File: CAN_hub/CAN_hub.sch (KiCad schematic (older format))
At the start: 8 parts, among them J1 Conn_01x04_Male, J2 Conn_01x04_Male, J3 Conn_01x04_Male, J4 Conn_01x04_Male, J5 Conn_01x04_Male, J6 Conn_01x04_Male, J7 Conn_01x04_Male, J8 Conn_01x04_Male

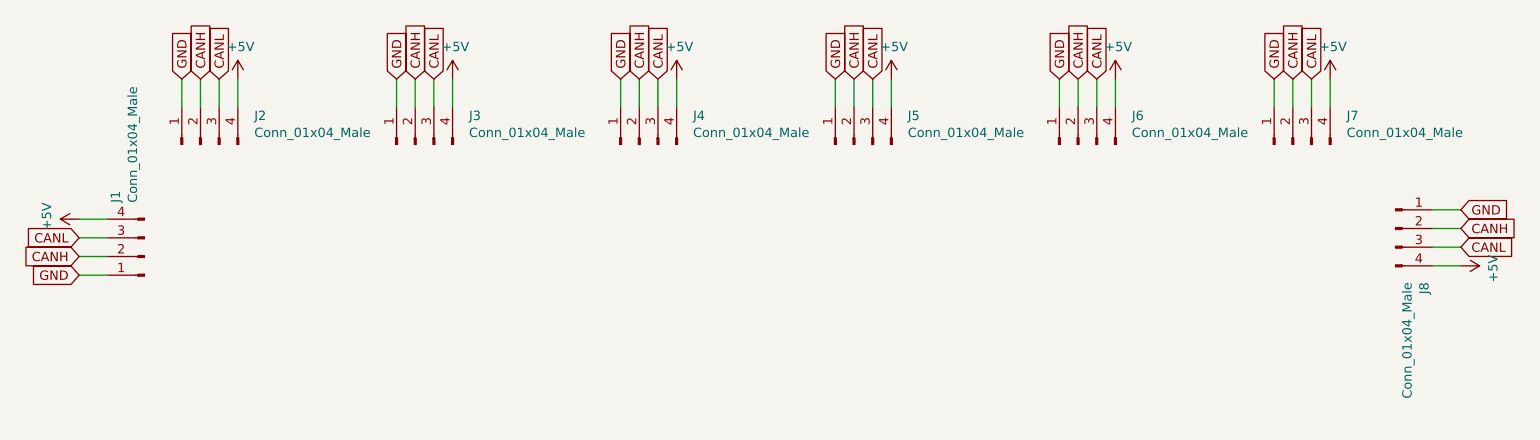
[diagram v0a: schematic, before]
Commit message: Updated shematic and layout to accomodate changes from first round of testing
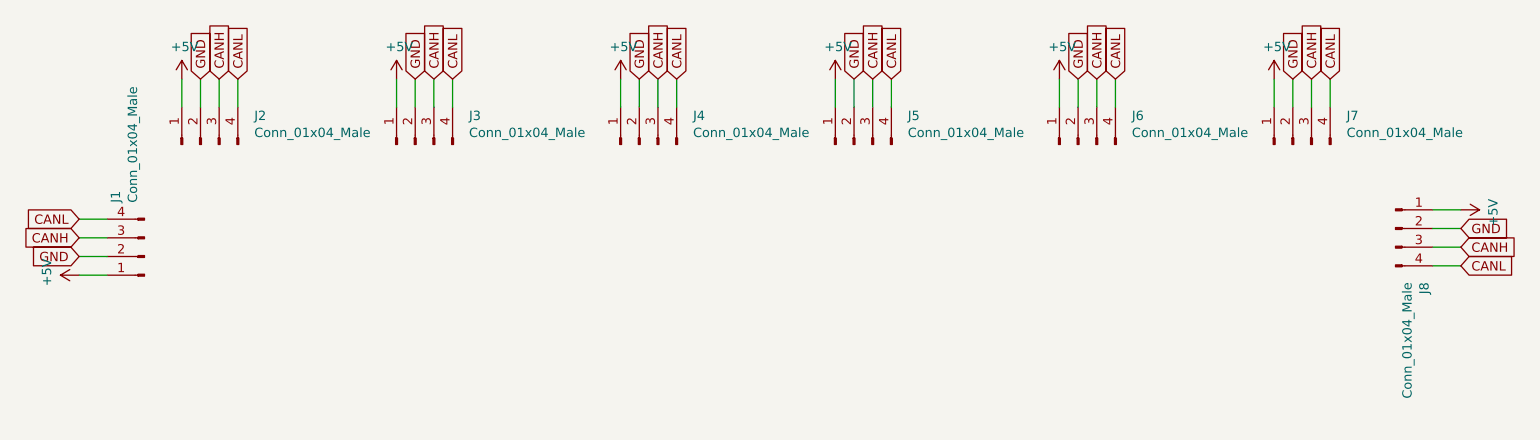
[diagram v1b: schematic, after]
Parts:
- J1, J2, J3, J4, J5, J6, J7, J8: footprint Connector_PinHeader_1.00mm:PinHeader_1x04_P1.00mm_Vertical -> Connector_JST:JST_EH_B4B-EH-A_1x04_P2.50mm_Vertical
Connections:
- net +5V: now also J1.1 (Pin_1), J2.1 (Pin_1), J3.1 (Pin_1), J4.1 (Pin_1), J5.1 (Pin_1), J6.1 (Pin_1), J7.1 (Pin_1), J8.1 (Pin_1); no longer J1.4 (Pin_4), J2.4 (Pin_4), J3.4 (Pin_4), J4.4 (Pin_4), J5.4 (Pin_4), J6.4 (Pin_4), J7.4 (Pin_4), J8.4 (Pin_4)
- net CANH: now also J1.3 (Pin_3), J2.3 (Pin_3), J3.3 (Pin_3), J4.3 (Pin_3), J5.3 (Pin_3), J6.3 (Pin_3), J7.3 (Pin_3), J8.3 (Pin_3); no longer J1.2 (Pin_2), J2.2 (Pin_2), J3.2 (Pin_2), J4.2 (Pin_2), J5.2 (Pin_2), J6.2 (Pin_2), J7.2 (Pin_2), J8.2 (Pin_2)
- net CANL: now also J1.4 (Pin_4), J2.4 (Pin_4), J3.4 (Pin_4), J4.4 (Pin_4), J5.4 (Pin_4), J6.4 (Pin_4), J7.4 (Pin_4), J8.4 (Pin_4); no longer J1.3 (Pin_3), J2.3 (Pin_3), J3.3 (Pin_3), J4.3 (Pin_3), J5.3 (Pin_3), J6.3 (Pin_3), J7.3 (Pin_3), J8.3 (Pin_3)
- net GND: now also J1.2 (Pin_2), J2.2 (Pin_2), J3.2 (Pin_2), J4.2 (Pin_2), J5.2 (Pin_2), J6.2 (Pin_2), J7.2 (Pin_2), J8.2 (Pin_2); no longer J1.1 (Pin_1), J2.1 (Pin_1), J3.1 (Pin_1), J4.1 (Pin_1), J5.1 (Pin_1), J6.1 (Pin_1), J7.1 (Pin_1), J8.1 (Pin_1)
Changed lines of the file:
@@
 EESchema Schematic File Version 4
-LIBS:CAN_8_connectors-cache
+LIBS:CAN_hub-cache
 EELAYER 30 0
 EELAYER END
@@
 Wire Wire Line
 	3700 2600 3700 2750
-Text GLabel 3700 2600 1    50   Input ~ 0
+Text GLabel 3800 2600 1    50   Input ~ 0
 GND
 $Comp
@@
 F 0 "J3" V 3954 2662 50  0000 R CNN
 F 1 "Conn_01x04_Male" V 3863 2662 50  0000 R CNN
-F 2 "Connector_PinHeader_1.00mm:PinHeader_1x04_P1.00mm_Vertical" H 3800 2950 50  0001 C CNN
+F 2 "Connector_JST:JST_EH_B4B-EH-A_1x04_P2.50mm_Vertical" H 3800 2950 50  0001 C CNN
 F 3 "~" H 3800 2950 50  0001 C CNN
 	1    3800 2950
 	0    -1   -1   0
 $EndComp
-Text GLabel 3800 2600 1    50   Input ~ 0
-CANH
 Text GLabel 3900 2600 1    50   Input ~ 0
+CANH
+Text GLabel 4000 2600 1    50   Input ~ 0
 CANL
 Wire Wire Line
@@
 L power:+5V #PWR03
 U 1 1 5E38804E
-P 4000 2600
-F 0 "#PWR03" H 4000 2450 50  0001 C CNN
-F 1 "+5V" H 4015 2773 50  0000 C CNN
-F 2 "" H 4000 2600 50  0001 C CNN
-F 3 "" H 4000 2600 50  0001 C CNN
-	1    4000 2600
+P 3700 2600
+F 0 "#PWR03" H 3700 2450 50  0001 C CNN
+F 1 "+5V" H 3715 2773 50  0000 C CNN
+F 2 "" H 3700 2600 50  0001 C CNN
+F 3 "" H 3700 2600 50  0001 C CNN
+	1    3700 2600
 	1    0    0    -1
 $EndComp
 Wire Wire Line
 	4000 2600 4000 2750
-Text GLabel 2550 2600 1    50   Input ~ 0
-GND
 Text GLabel 2650 2600 1    50   Input ~ 0
-CANH
+GND
 Text GLabel 2750 2600 1    50   Input ~ 0
+CANH
+Text GLabel 2850 2600 1    50   Input ~ 0
 CANL
 $Comp
 L power:+5V #PWR02
 U 1 1 5E370C49
-P 2850 2600
-F 0 "#PWR02" H 2850 2450 50  0001 C CNN
-F 1 "+5V" H 2865 2773 50  0000 C CNN
-F 2 "" H 2850 2600 50  0001 C CNN
-F 3 "" H 2850 2600 50  0001 C CNN
-	1    2850 2600
+P 2550 2600
+F 0 "#PWR02" H 2550 2450 50  0001 C CNN
+F 1 "+5V" H 2565 2773 50  0000 C CNN
+F 2 "" H 2550 2600 50  0001 C CNN
+F 3 "" H 2550 2600 50  0001 C CNN
+	1    2550 2600
 	1    0    0    -1
 $EndComp
@@
 F 0 "J2" V 2804 2662 50  0000 R CNN
 F 1 "Conn_01x04_Male" V 2713 2662 50  0000 R CNN
-F 2 "Connector_PinHeader_1.00mm:PinHeader_1x04_P1.00mm_Vertical" H 2650 2950 50  0001 C CNN
+F 2 "Connector_JST:JST_EH_B4B-EH-A_1x04_P2.50mm_Vertical" H 2650 2950 50  0001 C CNN
 F 3 "~" H 2650 2950 50  0001 C CNN
 	1    2650 2950
@@
 Wire Wire Line
 	2550 2600 2550 2750
-Wire Wire Line
-	6050 2600 6050 2750
-Text GLabel 6050 2600 1    50   Input ~ 0
+Text GLabel 6150 2600 1    50   Input ~ 0
 GND
 $Comp
@@
 F 0 "J5" V 6304 2662 50  0000 R CNN
 F 1 "Conn_01x04_Male" V 6213 2662 50  0000 R CNN
-F 2 "Connector_PinHeader_1.00mm:PinHeader_1x04_P1.00mm_Vertical" H 6150 2950 50  0001 C CNN
+F 2 "Connector_JST:JST_EH_B4B-EH-A_1x04_P2.50mm_Vertical" H 6150 2950 50  0001 C CNN
 F 3 "~" H 6150 2950 50  0001 C CNN
 	1    6150 2950
 	0    -1   -1   0
 $EndComp
-Text GLabel 6150 2600 1    50   Input ~ 0
-CANH
 Text GLabel 6250 2600 1    50   Input ~ 0
+CANH
+Text GLabel 6350 2600 1    50   Input ~ 0
 CANL
 Wire Wire Line
@@
 L power:+5V #PWR05
 U 1 1 5E3B06D8
-P 6350 2600
-F 0 "#PWR05" H 6350 2450 50  0001 C CNN
-F 1 "+5V" H 6365 2773 50  0000 C CNN
-F 2 "" H 6350 2600 50  0001 C CNN
-F 3 "" H 6350 2600 50  0001 C CNN
-	1    6350 2600
+P 6050 2600
+F 0 "#PWR05" H 6050 2450 50  0001 C CNN
+F 1 "+5V" H 6065 2773 50  0000 C CNN
+F 2 "" H 6050 2600 50  0001 C CNN
+F 3 "" H 6050 2600 50  0001 C CNN
+	1    6050 2600
 	1    0    0    -1
 $EndComp
 Wire Wire Line
 	6350 2600 6350 2750
-Text GLabel 4900 2600 1    50   Input ~ 0
-GND
 Text GLabel 5000 2600 1    50   Input ~ 0
-CANH
+GND
 Text GLabel 5100 2600 1    50   Input ~ 0
+CANH
+Text GLabel 5200 2600 1    50   Input ~ 0
 CANL
 $Comp
 L power:+5V #PWR04
 U 1 1 5E3B06E2
-P 5200 2600
-F 0 "#PWR04" H 5200 2450 50  0001 C CNN
-F 1 "+5V" H 5215 2773 50  0000 C CNN
-F 2 "" H 5200 2600 50  0001 C CNN
-F 3 "" H 5200 2600 50  0001 C CNN
-	1    5200 2600
+P 4900 2600
+F 0 "#PWR04" H 4900 2450 50  0001 C CNN
+F 1 "+5V" H 4915 2773 50  0000 C CNN
+F 2 "" H 4900 2600 50  0001 C CNN
+F 3 "" H 4900 2600 50  0001 C CNN
+	1    4900 2600
 	1    0    0    -1
 $EndComp
@@
 F 0 "J4" V 5154 2662 50  0000 R CNN
 F 1 "Conn_01x04_Male" V 5063 2662 50  0000 R CNN
-F 2 "Connector_PinHeader_1.00mm:PinHeader_1x04_P1.00mm_Vertical" H 5000 2950 50  0001 C CNN
+F 2 "Connector_JST:JST_EH_B4B-EH-A_1x04_P2.50mm_Vertical" H 5000 2950 50  0001 C CNN
 F 3 "~" H 5000 2950 50  0001 C CNN
 	1    5000 2950
@@
 Wire Wire Line
 	8400 2600 8400 2750
-Text GLabel 8400 2600 1    50   Input ~ 0
+Text GLabel 8500 2600 1    50   Input ~ 0
 GND
 $Comp
@@
 F 0 "J7" V 8654 2662 50  0000 R CNN
 F 1 "Conn_01x04_Male" V 8563 2662 50  0000 R CNN
-F 2 "Connector_PinHeader_1.00mm:PinHeader_1x04_P1.00mm_Vertical" H 8500 2950 50  0001 C CNN
+F 2 "Connector_JST:JST_EH_B4B-EH-A_1x04_P2.50mm_Vertical" H 8500 2950 50  0001 C CNN
 F 3 "~" H 8500 2950 50  0001 C CNN
 	1    8500 2950
 	0    -1   -1   0
 $EndComp
-Text GLabel 8500 2600 1    50   Input ~ 0
-CANH
 Text GLabel 8600 2600 1    50   Input ~ 0
+CANH
+Text GLabel 8700 2600 1    50   Input ~ 0
 CANL
 Wire Wire Line
@@
 L power:+5V #PWR07
 U 1 1 5E3B175A
-P 8700 2600
-F 0 "#PWR07" H 8700 2450 50  0001 C CNN
-F 1 "+5V" H 8715 2773 50  0000 C CNN
-F 2 "" H 8700 2600 50  0001 C CNN
-F 3 "" H 8700 2600 50  0001 C CNN
-	1    8700 2600
+P 8400 2600
+F 0 "#PWR07" H 8400 2450 50  0001 C CNN
+F 1 "+5V" H 8415 2773 50  0000 C CNN
+F 2 "" H 8400 2600 50  0001 C CNN
+F 3 "" H 8400 2600 50  0001 C CNN
+	1    8400 2600
 	1    0    0    -1
 $EndComp
 Wire Wire Line
 	8700 2600 8700 2750
-Text GLabel 7250 2600 1    50   Input ~ 0
-GND
 Text GLabel 7350 2600 1    50   Input ~ 0
-CANH
+GND
 Text GLabel 7450 2600 1    50   Input ~ 0
+CANH
+Text GLabel 7550 2600 1    50   Input ~ 0
 CANL
 $Comp
 L power:+5V #PWR06
 U 1 1 5E3B1764
-P 7550 2600
-F 0 "#PWR06" H 7550 2450 50  0001 C CNN
-F 1 "+5V" H 7565 2773 50  0000 C CNN
-F 2 "" H 7550 2600 50  0001 C CNN
-F 3 "" H 7550 2600 50  0001 C CNN
-	1    7550 2600
+P 7250 2600
+F 0 "#PWR06" H 7250 2450 50  0001 C CNN
+F 1 "+5V" H 7265 2773 50  0000 C CNN
+F 2 "" H 7250 2600 50  0001 C CNN
+F 3 "" H 7250 2600 50  0001 C CNN
+	1    7250 2600
 	1    0    0    -1
 $EndComp
@@
 F 0 "J6" V 7504 2662 50  0000 R CNN
 F 1 "Conn_01x04_Male" V 7413 2662 50  0000 R CNN
-F 2 "Connector_PinHeader_1.00mm:PinHeader_1x04_P1.00mm_Vertical" H 7350 2950 50  0001 C CNN
+F 2 "Connector_JST:JST_EH_B4B-EH-A_1x04_P2.50mm_Vertical" H 7350 2950 50  0001 C CNN
 F 3 "~" H 7350 2950 50  0001 C CNN
 	1    7350 2950
@@
 Wire Wire Line
 	7250 2600 7250 2750
-Text GLabel 2000 3650 0    50   Input ~ 0
-GND
 Text GLabel 2000 3550 0    50   Input ~ 0
-CANH
+GND
 Text GLabel 2000 3450 0    50   Input ~ 0
+CANH
+Text GLabel 2000 3350 0    50   Input ~ 0
 CANL
 $Comp
 L power:+5V #PWR01
 U 1 1 5E3B2F0E
-P 2000 3350
-F 0 "#PWR01" H 2000 3200 50  0001 C CNN
-F 1 "+5V" H 2015 3523 50  0000 C CNN
-F 2 "" H 2000 3350 50  0001 C CNN
-F 3 "" H 2000 3350 50  0001 C CNN
-	1    2000 3350
+P 2000 3650
+F 0 "#PWR01" H 2000 3500 50  0001 C CNN
+F 1 "+5V" H 2015 3823 50  0000 C CNN
+F 2 "" H 2000 3650 50  0001 C CNN
+F 3 "" H 2000 3650 50  0001 C CNN
+	1    2000 3650
 	0    -1   -1   0
 $EndComp
@@
 F 0 "J1" V 2504 3262 50  0000 R CNN
 F 1 "Conn_01x04_Male" V 2413 3262 50  0000 R CNN
-F 2 "Connector_PinHeader_1.00mm:PinHeader_1x04_P1.00mm_Vertical" H 2350 3550 50  0001 C CNN
+F 2 "Connector_JST:JST_EH_B4B-EH-A_1x04_P2.50mm_Vertical" H 2350 3550 50  0001 C CNN
 F 3 "~" H 2350 3550 50  0001 C CNN
 	1    2350 3550
@@
 Wire Wire Line
 	2000 3650 2150 3650
-Text GLabel 9400 3300 2    50   Input ~ 0
-GND
 Text GLabel 9400 3400 2    50   Input ~ 0
-CANH
+GND
 Text GLabel 9400 3500 2    50   Input ~ 0
+CANH
+Text GLabel 9400 3600 2    50   Input ~ 0
 CANL
 $Comp
 L power:+5V #PWR08
 U 1 1 5E3B4D45
-P 9400 3600
-F 0 "#PWR08" H 9400 3450 50  0001 C CNN
-F 1 "+5V" H 9415 3773 50  0000 C CNN
-F 2 "" H 9400 3600 50  0001 C CNN
-F 3 "" H 9400 3600 50  0001 C CNN
-	1    9400 3600
+P 9400 3300
+F 0 "#PWR08" H 9400 3150 50  0001 C CNN
+F 1 "+5V" H 9415 3473 50  0000 C CNN
+F 2 "" H 9400 3300 50  0001 C CNN
+F 3 "" H 9400 3300 50  0001 C CNN
+	1    9400 3300
 	0    1    1    0
 $EndComp
@@
 F 0 "J8" V 9204 3112 50  0000 R CNN
 F 1 "Conn_01x04_Male" V 9113 3112 50  0000 R CNN
-F 2 "Connector_PinHeader_1.00mm:PinHeader_1x04_P1.00mm_Vertical" H 9050 3400 50  0001 C CNN
+F 2 "Connector_JST:JST_EH_B4B-EH-A_1x04_P2.50mm_Vertical" H 9050 3400 50  0001 C CNN
 F 3 "~" H 9050 3400 50  0001 C CNN
 	1    9050 3400
@@
 Wire Wire Line
 	9400 3300 9250 3300
+Wire Wire Line
+	6050 2600 6050 2750
 $EndSCHEMATC
